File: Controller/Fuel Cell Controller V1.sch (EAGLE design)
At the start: 8 parts

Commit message: update
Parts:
- removed H2BOARD1: ETHERNET, ETHERNET:ETHERNET
- added CVM, POWERBOARD, PRESSURE, RELAY1, RELAY2: ETHERNET, ETHERNET:ETHERNET
- added FRAME2: FRAME-LETTERNO_PACKAGE, SparkFun-Aesthetics:FRAME-LETTERNO_PACKAGE
- added U$5: RS232-TO-CAN-CONVERTER, rs232-to-can:RS232-TO-CAN-CONVERTER
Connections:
- removed net 12V_AUX: H2BOARD.6
- removed net FC_R: H2BOARD1.6
- removed net MISO: U$1.12/MISO
- removed net MOSI: U$1.11/MOSI
- removed net SCK: U$1.13/SCK/LED
- new net AUX12: H2BOARD.6, POWERBOARD.3, RELAY1.5
- new net CAP_R: RELAY1.3, U$1.11/MOSI
- new net CHARGE_R: RELAY1.4, U$1.12/MISO
- new net EXTRA_V: U$1.10/TX2/PWM
- new net FC12: POWERBOARD.1, POWERBOARD.2, PRESSURE.1, RELAY1.6
- new net FCC_R: POWERBOARD.8, RELAY2.6, U$1.20/A6/PWM
- new net FCPRES: PRESSURE.3, U$1.23/A9/T/PWM
- new net MOTOR_R: RELAY1.2, U$1.22/A8/T/PWM
- new net N$1: CVM.1
- new net N$2: CVM.2
- new net N$3: CVM.3
- new net N$4: CVM.4
- new net N$5: CVM.5
- new net N$6: CVM.6
- new net N$7: CVM.7
- new net N$8: CVM.8
- new net PURGE_V: U$1.9/RX2/PWM
- new net START_R: RELAY1.1, U$1.21/A7/PWM
- new net SUPPLY_V: U$1.6/PWM
- net 5V: now also POWERBOARD.4, RELAY2.5, U$5.+5V, U$5.VCC; no longer H2BOARD1.5
- net CAPCURR: now also RELAY2.1; no longer H2BOARD1.1
- net CAPVOLT: now also RELAY2.3; no longer H2BOARD1.3
- net FCCURR: now also RELAY2.2; no longer H2BOARD1.2
- net FCVOLT: now also RELAY2.4; no longer H2BOARD1.4
- net GND: now also CVM.SHD1, CVM.SHD2, POWERBOARD.5, POWERBOARD.6, POWERBOARD.7, POWERBOARD.SHD1, POWERBOARD.SHD2, PRESSURE.2, RELAY1.7, RELAY1.8, RELAY1.SHD1, RELAY1.SHD2, RELAY2.7, RELAY2.8, RELAY2.SHD1, RELAY2.SHD2, U$5.GND, U$5.GND_; no longer H2BOARD1.7, H2BOARD1.8, H2BOARD1.SHD1, H2BOARD1.SHD2
- net RX1: now also U$5.TX0
- net TX1: now also U$5.RXI
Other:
- note added: "Also requires a level converter"
- note added: "OPEN LOG"
- note added: "TO CAN"
- note added: "This pin out is completely wrong."

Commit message: update
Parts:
- removed POWERBOARD: ETHERNET, ETHERNET:ETHERNET
- added AUXPOWER, FCPOWER: 5555140-6, 5555140-6 RJ11:5555140-6
- added U$7: FAN-CONTROLLER, fan controller:FAN-CONTROLLER
- added U$8: MOSFETBOARD, mosfet board:MOSFETBOARD
- added VALVES: ETHERNET, ETHERNET:ETHERNET
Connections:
- removed net +5V: U$1.VIN
- new net AUX5: AUXPOWER.3, AUXPOWER.4, H2BOARD.8, U$5.+5V, U$5.VCC
- new net EXTRA_V_G: U$8.OUT3, VALVES.6
- new net FC5: FCPOWER.3, FCPOWER.4, U$1.VIN, U$2.RAW, U$7.5V, U$8.V+
- new net N$16: PRESSURE.4
- new net N$17: PRESSURE.5
- new net N$18: PRESSURE.6
- new net N$19: PRESSURE.7
- new net N$20: PRESSURE.8
- new net N$21: PRESSURE.SHD1
- new net N$22: PRESSURE.SHD2
- new net PURGE_V_G: U$8.OUT2, VALVES.4
- new net SUPPLY_V_G: U$8.OUT1, VALVES.2
- net +3.3V: no longer U$2.RAW
- net 5V: no longer H2BOARD.8, POWERBOARD.4, U$5.+5V, U$5.VCC
- net AUX12: now also AUXPOWER.1, AUXPOWER.2, VALVES.1; no longer POWERBOARD.3
- net EXTRA_V: now also U$8.IN3
- net FC12: now also FCPOWER.1, FCPOWER.2, U$7.12V, VALVES.3, VALVES.5; no longer POWERBOARD.1, POWERBOARD.2
- net FCC_R: no longer POWERBOARD.8
- net GND: now also AUXPOWER.5, AUXPOWER.6, AUXPOWER.SH1, AUXPOWER.SH2, FCPOWER.5, FCPOWER.6, FCPOWER.SH1, FCPOWER.SH2, U$7.GND, U$8.GND, VALVES.SHD1, VALVES.SHD2; no longer POWERBOARD.5, POWERBOARD.6, POWERBOARD.7, POWERBOARD.SHD1, POWERBOARD.SHD2
- net H2_OK: now also U$8.ESTOP
- net PURGE_V: now also U$8.IN2
- net SCL: now also U$7.SCL
- net SDA: now also U$7.SDA
- net SUPPLY_V: now also U$8.IN1
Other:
- moved on the sheet: U$1, U$4

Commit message: added rs 232 converter
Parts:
- added C1, C2, C3, C4: (no value), adafruit:C-USC0603
- added C41, C42, C44: 0.33uF/12V, E-P-008-R1.2:C-USC0805
- added C43: 0.047uF/12V, E-P-008-R1.2:C-USC0805
- added FRAME3, FRAME4: FRAME-LETTERNO_PACKAGE, SparkFun-Aesthetics:FRAME-LETTERNO_PACKAGE
- added ISP1: AVRISP-BOX, adafruit:AVRISP-BOX
- added R2: (no value), adafruit:R-US_R0603
- added U$6: EG4621CT-ND, EG4621CT-ND:EG4621CT-ND
- added U1: ATMEGA328P_TQFP, SparkFun-DigitalIC:ATMEGA328P_TQFP
- added U2: MAX3221CPWR, Texas Instruments_By_element14_Batch_1:MAX3221CPWR
- added Y1: (no value), SparkFun-FreqCtrl:CRYSTALHC49US
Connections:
- net N$5 renamed CVMSIG1
- net N$6 renamed CVMSIG2
- net N$7 renamed CVMSIG3
- net N$8 renamed CVMSIG4
- removed net N$1: CVM.1
- removed net N$2: CVM.2
- removed net N$3: CVM.3
- new net ATMEG_RESET: ISP1.RST, R2.1, U$6.P$2, U1.PC6(/RESET)
- new net CVMRX: U1.PD0(RXD), U2.ROUT
- new net CVMTX: U1.PD1(TXD), U2.DIN
- new net MISO: ISP1.MISO, U1.PB4(MISO)
- new net MOSI: ISP1.MOSI, U1.PB3(MOSI/OC2)
- new net N$5: C2.1, U1.PB7(XTAL2/TOSC2), Y1.1
- new net N$73: C41.1, U2.V+
- new net N$74: C43.1, U2.C1+
- new net N$75: C43.2, U2.C1-
- new net N$76: C44.1, U2.C2+
- new net N$77: C44.2, U2.C2-
- new net N$78: C42.1, U2.V-
- new net RX12: CVM.3, U2.RIN
- new net SCK: ISP1.SCK, U1.PB5(SCK)
- new net SER_INVALID: U2.~INVALID
- new net TX12: CVM.2, U2.DOUT
- new net V+: U2.~FORCEOFF
- net +3.3V: now also C3.1, C4.1, R2.2, U1.AREF, U1.AVCC, U1.VCC@4, U1.VCC@6, U2.VCC
- net FC5: now also CVM.1
- net GND: now also C1.2, C2.2, C3.2, C4.2, C41.2, C42.2, CVM.4, ISP1.GND, U$6.P$1, U1.AGND, U1.GND@3, U1.GND@5, U2.FORCEON, U2.GND, U2.~EN
- net N$4: now also C1.1, U1.PB6(XTAL1/TOSC1), Y1.2; no longer CVM.4
- net SCL: now also U1.PC5(ADC5/SCL)
- net SDA: now also U1.PC4(ADC4/SDA)
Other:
- note added: "Configured for auto shutdown"

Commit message: fcc schematic mostly done
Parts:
- added FRAME5, FRAME6: FRAME-LETTERNO_PACKAGE, SparkFun-Aesthetics:FRAME-LETTERNO_PACKAGE
- added U$9: LCD-BOARD, lcd board:LCD-BOARD
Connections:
- net +3.3V: now also U$5.VIN, U$9.V
- net GND: now also U$9.GND
- net SCL: now also U$9.SCL
- net SDA: now also U$9.SDA
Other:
- note added: "CAN Board runs at 5V"
- note added: "CAN Bus"
- note added: "CVM Board uses +/-12V rs232"
- note added: "Connections to Relay Board"
- note added: "Connections to power boards"
- note added: "Convert to 3.3V levels"
- note added: "DATA LOGGING"
- note added: "DISPLAY"
- note added: "FANS"
- note added: "H2 BOARD"
- note added: "Pressure Sensor"
- note added: "RTC"
- note added: "TEMP/HUMIDITY SENSOR"
- note added: "Teensy UART pins are 5V tollerant"
- note added: "Valves"
- note added: "aux"
- note added: "fc"
- note added: "over i2c"
- note added: "talk to main controller"
- note added: "then have atmega"
- note added: "to everything"
- note removed: "Also requires a level converter"
- note removed: "CHECK THIS PIN OUT"
- note removed: "This pin out is completely wrong."

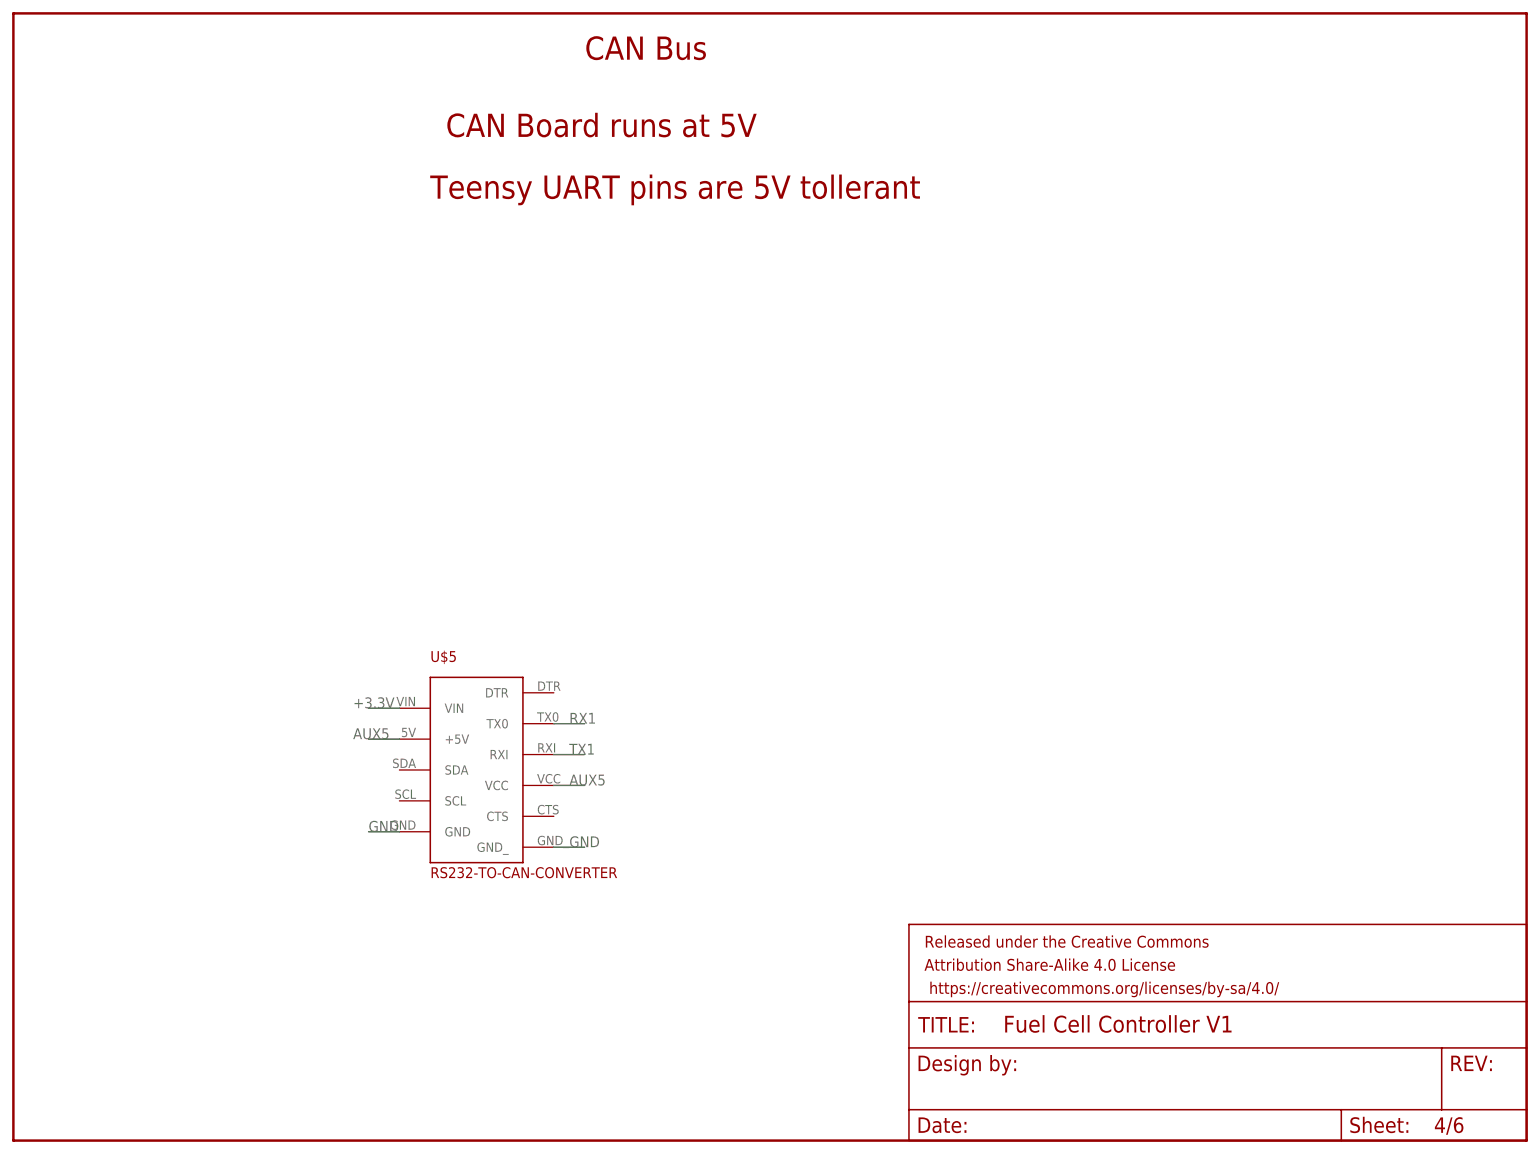
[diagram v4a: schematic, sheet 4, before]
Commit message: added connector for motor
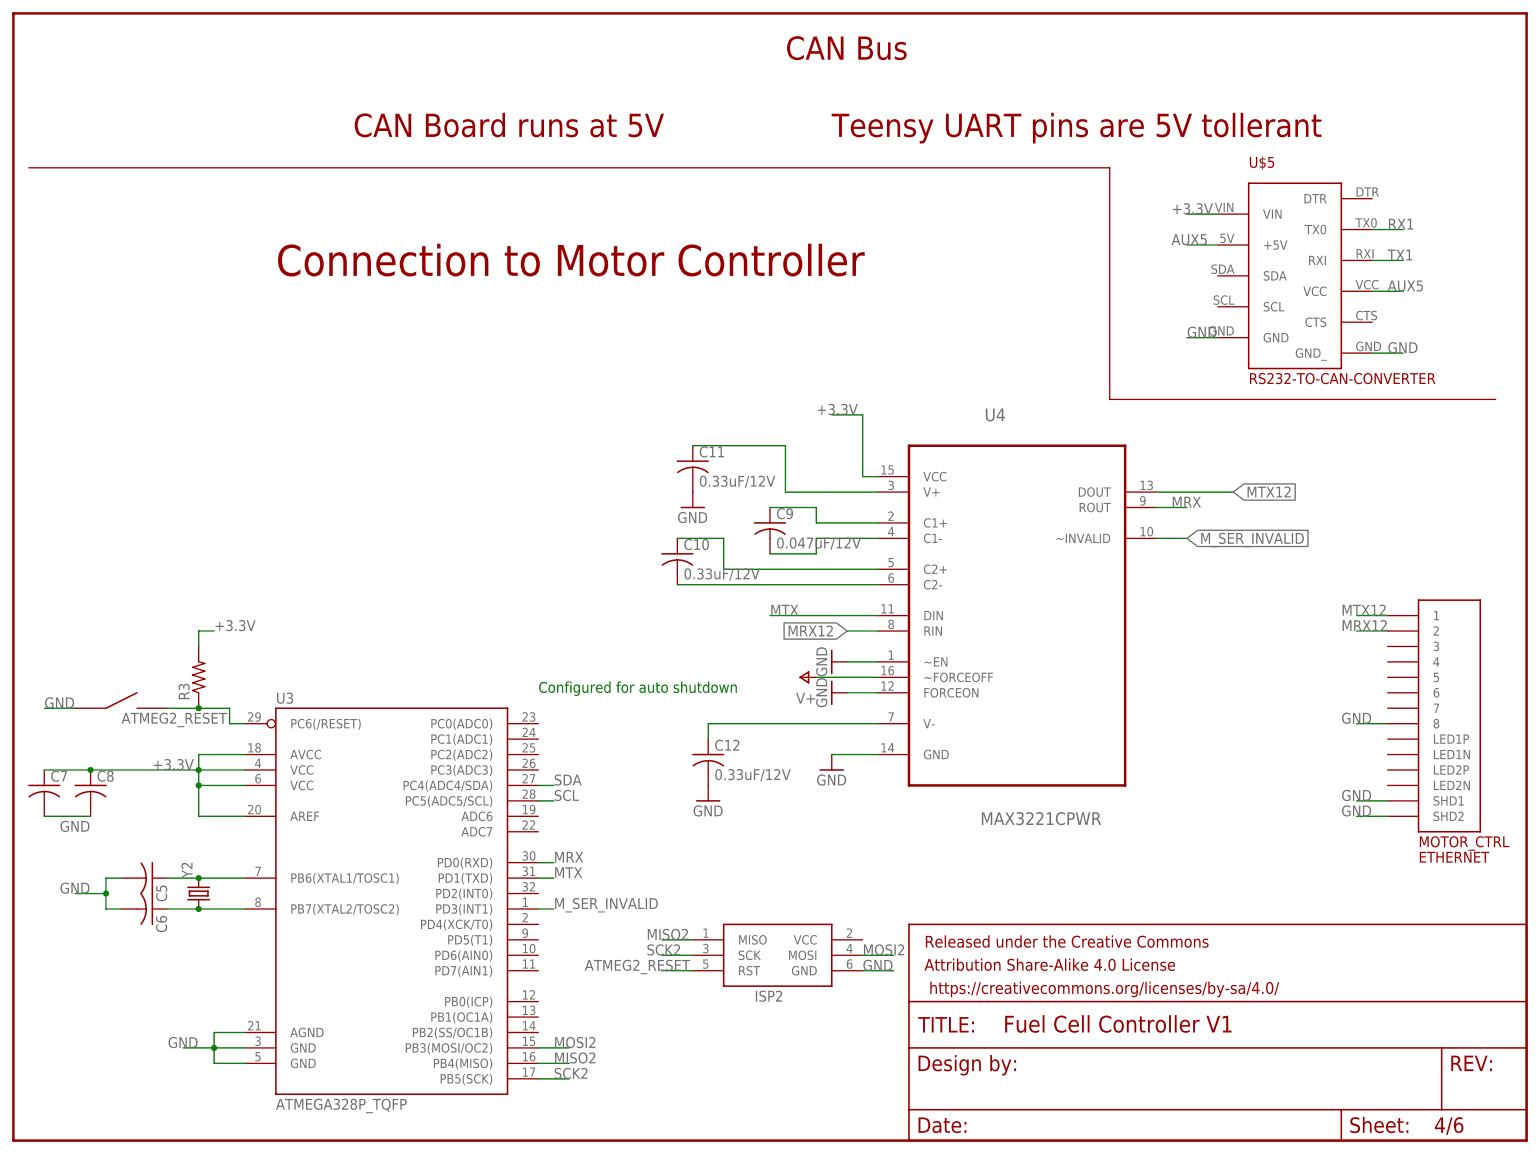
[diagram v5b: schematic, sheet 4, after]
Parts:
- added C10, C11, C12: 0.33uF/12V, E-P-008-R1.2:C-USC0805
- added C5, C6, C7, C8: (no value), adafruit:C-USC0603
- added C9: 0.047uF/12V, E-P-008-R1.2:C-USC0805
- added ISP2: AVRISP-BOX, adafruit:AVRISP-BOX
- added MOTOR_CTRL: ETHERNET, ETHERNET:ETHERNET
- added R3: (no value), adafruit:R-US_R0603
- added U$10: EG4621CT-ND, EG4621CT-ND:EG4621CT-ND
- added U3: ATMEGA328P_TQFP, SparkFun-DigitalIC:ATMEGA328P_TQFP
- added U4: MAX3221CPWR, Texas Instruments_By_element14_Batch_1:MAX3221CPWR
- added Y2: (no value), SparkFun-FreqCtrl:CRYSTALHC49US
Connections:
- net ATMEG_RESET renamed ATMEG1_RESET
- net MISO renamed MISO1
- net MOSI renamed MOSI1
- net RX12 renamed CVMRX12
- net SCK renamed SCK1
- net TX12 renamed CVMTX12
- removed net SER_INVALID: U2.~INVALID
- new net ATMEG2_RESET: ISP2.RST, R3.1, U$10.P$2, U3.PC6(/RESET)
- new net CVM_SER_INVALID: U1.PD3(INT1), U2.~INVALID
- new net GND1: ISP1.GND
- new net MISO2: ISP2.MISO, U3.PB4(MISO)
- new net MOSI2: ISP2.MOSI, U3.PB3(MOSI/OC2)
- new net MRX: U3.PD0(RXD), U4.ROUT
- new net MRX12: MOTOR_CTRL.2, U4.RIN
- new net MTX: U3.PD1(TXD), U4.DIN
- new net MTX12: MOTOR_CTRL.1, U4.DOUT
- new net M_SER_INVALID: U3.PD3(INT1), U4.~INVALID
- new net N$1: C5.1, U3.PB6(XTAL1/TOSC1), Y2.2
- new net N$10: C12.1, U4.V-
- new net N$2: C6.1, U3.PB7(XTAL2/TOSC2), Y2.1
- new net N$3: C11.1, U4.V+
- new net N$6: C9.1, U4.C1+
- new net N$7: C9.2, U4.C1-
- new net N$8: C10.1, U4.C2+
- new net N$9: C10.2, U4.C2-
- new net SCK2: ISP2.SCK, U3.PB5(SCK)
- net +3.3V: now also C7.1, C8.1, R3.2, U3.AREF, U3.AVCC, U3.VCC@4, U3.VCC@6, U4.VCC
- net GND: now also C11.2, C12.2, C5.2, C6.2, C7.2, C8.2, ISP2.GND, MOTOR_CTRL.8, MOTOR_CTRL.SHD1, MOTOR_CTRL.SHD2, U$10.P$1, U3.AGND, U3.GND@3, U3.GND@5, U4.FORCEON, U4.GND, U4.~EN; no longer ISP1.GND
- net SCL: now also U3.PC5(ADC5/SCL)
- net SDA: now also U3.PC4(ADC4/SDA)
- net V+: now also U4.~FORCEOFF
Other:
- note added: "Connection to Motor Controller"
- moved on the sheet: CVM, U$5

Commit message: update
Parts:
- added F1, F10, F2, F3, F4, F5, F6, F7, F8, F9: (no value), polyfuse:POLYFUSE
- added IC1: 4081D, 40xx:4081D
- added SJ1, SJ2: JUMPER-PAD-2-NC_BY_PASTE, SparkFun-Passives:JUMPER-PAD-2-NC_BY_PASTE
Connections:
- new net CAP_R_OUT: IC1C.O, RELAY1.3
- new net CHARGE_R_OUT: IC1D.O, RELAY1.4
- new net MOTOR_R_OUT: IC1B.O, RELAY1.2
- new net N$11: F1.2, H2BOARD.6
- new net N$12: F2.2, H2BOARD.8
- new net N$13: F3.2, U$7.5V
- new net N$14: F4.2, U$7.12V
- new net N$15: AUXPOWER.1, AUXPOWER.2, F5.2
- new net N$23: F6.1, U$1.VIN
- new net N$24: F7.2, FCPOWER.1, FCPOWER.2
- new net N$25: F8.2, FCPOWER.3, FCPOWER.4
- new net N$26: F9.1, U$1.3.3V
- new net N$27: CVM.1, F10.2
- new net START_R_OUT: IC1A.O, RELAY1.1
- new net VDD: SJ2.2
- new net VSS: SJ1.2
- net +3.3V: now also F9.2, SJ2.1; no longer U$1.3.3V
- net AUX12: now also F1.1, F5.1; no longer AUXPOWER.1, AUXPOWER.2, H2BOARD.6
- net AUX5: now also F2.1; no longer H2BOARD.8
- net CAP_R: now also IC1C.I0; no longer RELAY1.3
- net CHARGE_R: now also IC1D.I0; no longer RELAY1.4
- net EXTRA_SIG: now also U$1.5/PWM
- net FC12: now also F4.1, F7.1; no longer FCPOWER.1, FCPOWER.2, U$7.12V
- net FC5: now also F10.1, F3.1, F6.2, F8.1; no longer CVM.1, FCPOWER.3, FCPOWER.4, U$1.VIN, U$7.5V
- net GND: now also SJ1.1
- net H2_OK: now also IC1A.I1, IC1B.I1, IC1C.I1, IC1D.I1
- net MOTOR_R: now also IC1B.I0; no longer RELAY1.2
- net START_R: now also IC1A.I0; no longer RELAY1.1
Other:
- moved on the sheet: AUXPOWER, RELAY1, RELAY2
